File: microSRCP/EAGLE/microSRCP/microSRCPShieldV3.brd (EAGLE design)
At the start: 66.7 x 55.9 mm, 41 parts

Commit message: Feinkorrekturen
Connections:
- net S$10 renamed S$1
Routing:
- net GND: track 158.0 -> 159.5 mm
- net V5O: track 212.7 -> 212.1 mm
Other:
- board text added: "https://github.com/mc-b/microSRCP/wiki"
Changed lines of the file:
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@@
 <wire x1="66.675" y1="55.88" x2="0" y2="55.88" width="0.4064" layer="20"/>
 <wire x1="0" y1="55.88" x2="0" y2="0" width="0.4064" layer="20"/>
+<text x="19.685" y="48.26" size="1.27" layer="25">https://github.com/mc-b/microSRCP/wiki</text>
 </plain>
 <attributes>
@@
 <wire x1="12.7" y1="8.89" x2="5.08" y2="8.89" width="0.4064" layer="1"/>
 <wire x1="5.08" y1="8.89" x2="5.08" y2="10.16" width="0.4064" layer="1"/>
-<contactref element="LD4" pad="K"/>
-<wire x1="54.61" y1="20.32" x2="57.15" y2="27.94" width="0.4064" layer="1"/>
-<wire x1="57.15" y1="27.94" x2="53.34" y2="27.94" width="0.4064" layer="1"/>
-<contactref element="~LD5" pad="K"/>
-<wire x1="53.34" y1="27.94" x2="48.26" y2="27.94" width="0.4064" layer="1"/>
-<contactref element="~LD6" pad="K"/>
-<wire x1="48.26" y1="27.94" x2="43.18" y2="27.94" width="0.4064" layer="1"/>
-<contactref element="LD7" pad="K"/>
-<wire x1="43.18" y1="27.94" x2="38.1" y2="27.94" width="0.4064" layer="1"/>
+<wire x1="54.61" y1="20.32" x2="57.15" y2="20.32" width="0.4064" layer="1"/>
+<wire x1="57.15" y1="20.32" x2="57.15" y2="27.94" width="0.4064" layer="1"/>
+<contactref element="D0" pad="3"/>
 <wire x1="57.15" y1="27.94" x2="57.15" y2="33.02" width="0.4064" layer="1"/>
-<contactref element="D0" pad="3"/>
 <wire x1="57.15" y1="33.02" x2="57.15" y2="38.1" width="0.4064" layer="1"/>
 <wire x1="57.15" y1="38.1" x2="54.61" y2="38.1" width="0.4064" layer="1"/>
@@
 <contactref element="I2C" pad="4"/>
 <wire x1="57.15" y1="33.02" x2="59.69" y2="33.02" width="0.4064" layer="1"/>
+<contactref element="LD4" pad="K"/>
+<contactref element="~LD5" pad="K"/>
+<wire x1="53.34" y1="27.94" x2="48.26" y2="27.94" width="0.4064" layer="1"/>
+<contactref element="~LD6" pad="K"/>
+<wire x1="48.26" y1="27.94" x2="43.18" y2="27.94" width="0.4064" layer="1"/>
+<contactref element="LD7" pad="K"/>
+<wire x1="43.18" y1="27.94" x2="38.1" y2="27.94" width="0.4064" layer="1"/>
+<wire x1="53.34" y1="27.94" x2="57.15" y2="27.94" width="0.4064" layer="1"/>
 <contactref element="I2C-2" pad="4"/>
-<wire x1="54.61" y1="20.32" x2="59.69" y2="17.78" width="0.4064" layer="1"/>
+<wire x1="57.15" y1="20.32" x2="57.15" y2="17.78" width="0.4064" layer="1"/>
+<wire x1="57.15" y1="17.78" x2="59.69" y2="17.78" width="0.4064" layer="1"/>
 </signal>
 <signal name="V5O">
@@
 <wire x1="52.07" y1="17.78" x2="54.61" y2="17.78" width="0.4064" layer="1"/>
 <wire x1="39.37" y1="17.78" x2="41.91" y2="17.78" width="0.4064" layer="1"/>
-<wire x1="54.61" y1="17.78" x2="55.88" y2="17.78" width="0.4064" layer="16"/>
-<wire x1="55.88" y1="17.78" x2="57.15" y2="19.05" width="0.4064" layer="16"/>
-<wire x1="57.15" y1="19.05" x2="57.15" y2="30.48" width="0.4064" layer="16"/>
+<wire x1="54.61" y1="17.78" x2="57.15" y2="17.78" width="0.4064" layer="16"/>
+<wire x1="57.15" y1="17.78" x2="57.15" y2="30.48" width="0.4064" layer="16"/>
 <contactref element="D0" pad="2"/>
 <wire x1="57.15" y1="30.48" x2="57.15" y2="40.64" width="0.4064" layer="16"/>
@@
 <wire x1="11.43" y1="53.34" x2="11.43" y2="50.8" width="0.4064" layer="1"/>
 <contactref element="I2C-2" pad="3"/>
-<wire x1="57.15" y1="19.05" x2="57.15" y2="17.78" width="0.4064" layer="16"/>
 <wire x1="57.15" y1="17.78" x2="59.69" y2="15.24" width="0.4064" layer="16"/>
 <contactref element="I2C" pad="3"/>
@@
 <contactref element="LD4" pad="A"/>
 <wire x1="44.45" y1="35.56" x2="53.34" y2="30.48" width="0.4064" layer="16"/>
-</signal>
-<signal name="S$10">
-<contactref element="R2" pad="P$1"/>
-<contactref element="~LD5" pad="A"/>
-<wire x1="41.91" y1="35.56" x2="48.26" y2="30.48" width="0.4064" layer="16"/>
 </signal>
 <signal name="S$11">
@@
 <wire x1="15.24" y1="38.1" x2="15.24" y2="40.64" width="0.4064" layer="16"/>
 </signal>
+<signal name="S$1">
+<contactref element="R2" pad="P$1"/>
+<contactref element="~LD5" pad="A"/>
+<wire x1="41.91" y1="35.56" x2="46.99" y2="30.48" width="0.4064" layer="16"/>
+<wire x1="46.99" y1="30.48" x2="48.26" y2="30.48" width="0.4064" layer="16"/>
+</signal>
 </signals>

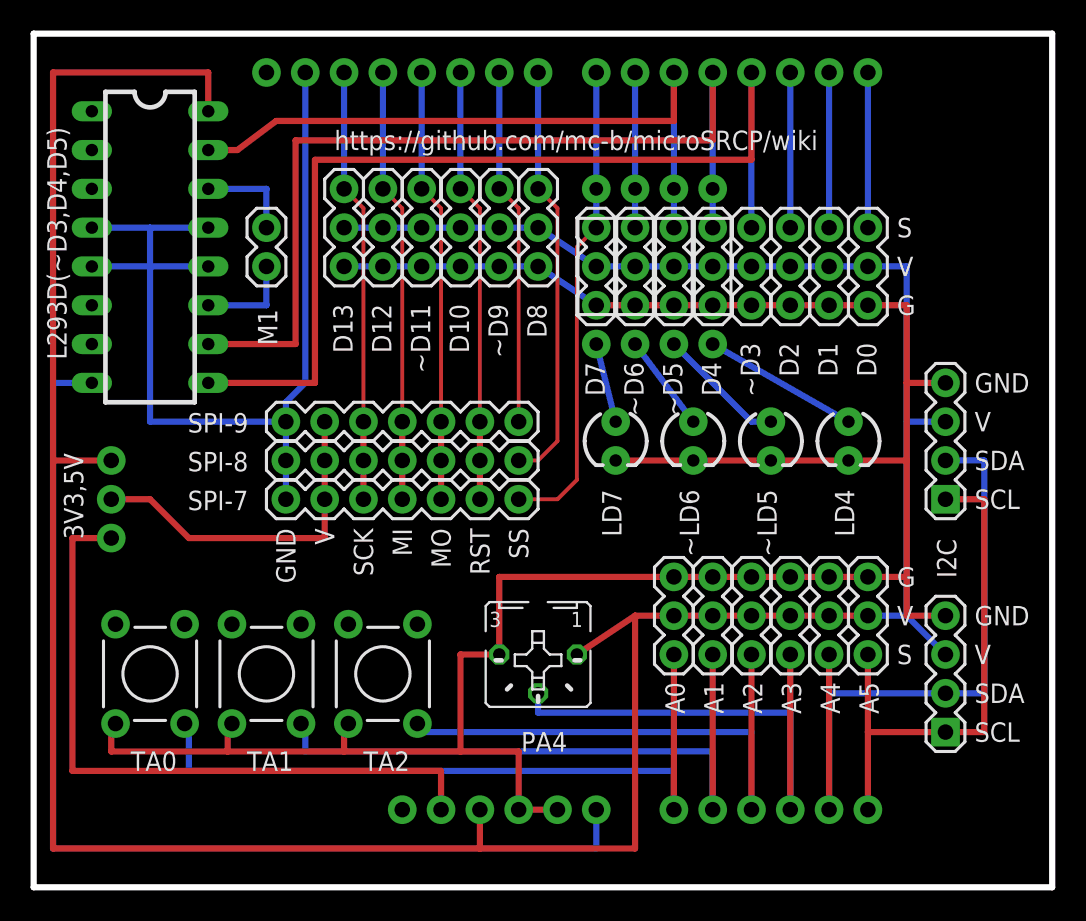
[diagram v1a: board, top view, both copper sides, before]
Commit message: V3 mit gleicher Pin-Belegung wie V2 plus SPI Anschluessen
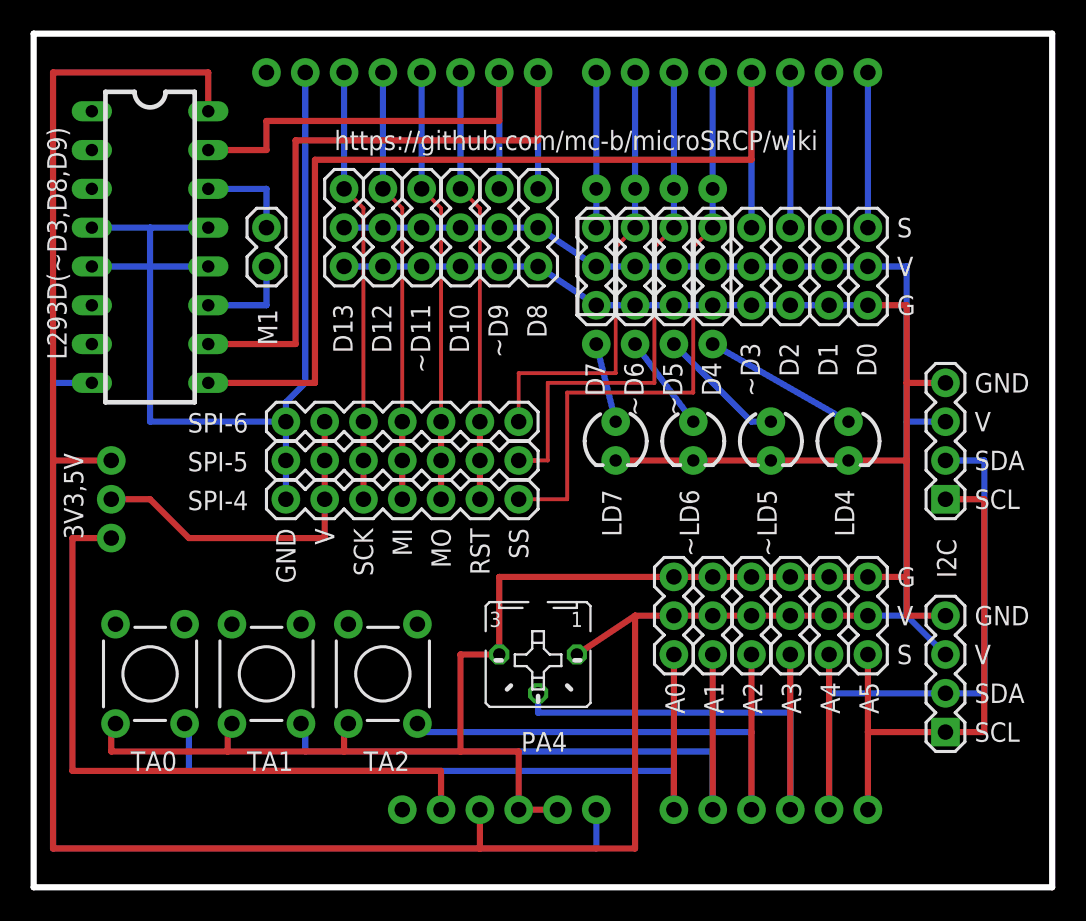
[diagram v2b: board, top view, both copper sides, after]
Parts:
- renumbered L293D(~D3,D4,D5) to L293D(~D3,D8,D9), SPI-7 to SPI-4, SPI-8 to SPI-5, SPI-9 to SPI-6
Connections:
- removed net S4: D4.1, E$1.D4, L293D(~D3,D8,D9).10, R3.P$2
- removed net S9: E$1.D9, SPI-6.7, ~D9.1
- new net S$3: E$1.D9, L293D(~D3,D8,D9).15, ~D9.1
- new net S$4: D4.1, E$1.D4, R3.P$2, SPI-4.7
- net S5: now also SPI-5.7; no longer L293D(~D3,D8,D9).15
- net S6: now also SPI-6.7
- net S7: no longer SPI-4.7
- net S8: now also L293D(~D3,D8,D9).10; no longer SPI-5.7
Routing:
- net S4: track 61.0 -> 0.00 mm
- net S$4: track 0.00 -> 39.9 mm
- net S$3: track 0.00 -> 31.8 mm
- net S9: track 23.4 -> 0.00 mm
- net S7: track 31.5 -> 10.2 mm
- net S6: track 10.2 -> 29.7 mm
- net S8: track 27.7 -> 47.0 mm
- net S5: track 44.5 -> 36.1 mm

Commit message: Massenflaechen angefuegt
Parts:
- renumbered D10 to ~D10
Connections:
- removed net GND1: E$1.GND@2, L293D(~D3,D8,D9).12, L293D(~D3,D8,D9).13, L293D(~D3,D8,D9).4, L293D(~D3,D8,D9).5, SPI-4.1, SPI-5.1, SPI-6.1
- net GND: now also E$1.GND@2, L293D(~D3,D8,D9).12, L293D(~D3,D8,D9).13, L293D(~D3,D8,D9).4, L293D(~D3,D8,D9).5, SPI-4.1, SPI-5.1, SPI-6.1
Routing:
- net GND: track 159.5 -> 227.4 mm
- net GND1: track 65.3 -> 0.00 mm
- added copper zone on layer 1, net GND
- added copper zone on layer 16, net GND
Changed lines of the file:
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@@
 <layers>
 <layer number="1" name="Top" color="4" fill="1" visible="yes" active="yes"/>
-<layer number="16" name="Bottom" color="1" fill="1" visible="yes" active="yes"/>
+<layer number="16" name="Bottom" color="1" fill="1" visible="no" active="yes"/>
 <layer number="17" name="Pads" color="2" fill="1" visible="yes" active="yes"/>
 <layer number="18" name="Vias" color="2" fill="1" visible="yes" active="yes"/>
@@
 <attribute name="VALUE" x="27.305" y="46.99" size="1.27" layer="27" rot="R270"/>
 </element>
-<element name="D10" library="SparkFun-Connectors" package="1X03" value="" x="27.94" y="45.72" smashed="yes" rot="R270">
+<element name="~D10" library="SparkFun-Connectors" package="1X03" value="" x="27.94" y="45.72" smashed="yes" rot="R270">
 <attribute name="NAME" x="27.2288" y="38.1762" size="1.27" layer="25" ratio="10" rot="R270"/>
 <attribute name="VALUE" x="24.765" y="46.99" size="1.27" layer="27" rot="R270"/>
@@
 <contactref element="~D9" pad="3"/>
 <wire x1="33.02" y1="40.64" x2="30.48" y2="40.64" width="0.4064" layer="16"/>
-<contactref element="D10" pad="3"/>
+<contactref element="~D10" pad="3"/>
 <wire x1="30.48" y1="40.64" x2="27.94" y2="40.64" width="0.4064" layer="16"/>
 <contactref element="~D11" pad="3"/>
@@
 <wire x1="22.86" y1="40.64" x2="20.32" y2="40.64" width="0.4064" layer="16"/>
 <wire x1="39.37" y1="38.1" x2="36.83" y2="38.1" width="0.4064" layer="16"/>
+<polygon width="0.4064" layer="16">
+<vertex x="0.635" y="54.61"/>
+<vertex x="0.635" y="1.27"/>
+<vertex x="65.405" y="1.27"/>
+<vertex x="65.405" y="54.61"/>
+</polygon>
+<contactref element="E$1" pad="GND@2"/>
+<wire x1="17.78" y1="53.34" x2="17.78" y2="40.64" width="0.4064" layer="16"/>
+<contactref element="SPI-6" pad="1"/>
+<wire x1="17.78" y1="40.64" x2="17.78" y2="33.02" width="0.4064" layer="16"/>
+<wire x1="17.78" y1="33.02" x2="16.51" y2="31.75" width="0.4064" layer="16"/>
+<wire x1="16.51" y1="31.75" x2="16.51" y2="30.48" width="0.4064" layer="16"/>
+<contactref element="SPI-5" pad="1"/>
+<wire x1="16.51" y1="30.48" x2="16.51" y2="27.94" width="0.4064" layer="16"/>
+<contactref element="SPI-4" pad="1"/>
+<wire x1="16.51" y1="27.94" x2="16.51" y2="25.4" width="0.4064" layer="16"/>
+<wire x1="16.51" y1="30.48" x2="7.62" y2="30.48" width="0.4064" layer="16"/>
+<wire x1="7.62" y1="30.48" x2="7.62" y2="40.64" width="0.4064" layer="16"/>
+<contactref element="L293D(~D3,D8,D9)" pad="12"/>
+<wire x1="11.43" y1="40.64" x2="7.62" y2="40.64" width="0.4064" layer="16"/>
+<contactref element="L293D(~D3,D8,D9)" pad="13"/>
+<contactref element="L293D(~D3,D8,D9)" pad="4"/>
+<wire x1="11.43" y1="43.18" x2="7.62" y2="43.18" width="0.4064" layer="16"/>
+<wire x1="3.81" y1="43.18" x2="7.62" y2="43.18" width="0.4064" layer="16"/>
+<wire x1="7.62" y1="43.18" x2="7.62" y2="40.64" width="0.4064" layer="16"/>
+<contactref element="L293D(~D3,D8,D9)" pad="5"/>
+<wire x1="7.62" y1="40.64" x2="3.81" y2="40.64" width="0.4064" layer="16"/>
+<wire x1="17.78" y1="40.64" x2="20.32" y2="40.64" width="0.4064" layer="16"/>
+<polygon width="0.4064" layer="1">
+<vertex x="0.635" y="55.245"/>
+<vertex x="0.635" y="1.27"/>
+<vertex x="65.405" y="1.27"/>
+<vertex x="65.405" y="1.905"/>
+<vertex x="65.405" y="55.245"/>
+</polygon>
 </signal>
 <signal name="V5O">
@@
 <contactref element="~D9" pad="2"/>
 <wire x1="33.02" y1="43.18" x2="30.48" y2="43.18" width="0.4064" layer="16"/>
-<contactref element="D10" pad="2"/>
+<contactref element="~D10" pad="2"/>
 <wire x1="30.48" y1="43.18" x2="27.94" y2="43.18" width="0.4064" layer="16"/>
 <contactref element="~D11" pad="2"/>
@@
 <wire x1="39.37" y1="53.34" x2="39.37" y2="43.18" width="0.4064" layer="16"/>
 <contactref element="~D6" pad="1"/>
-<wire x1="39.37" y1="43.18" x2="39.37" y2="45.72" width="0" layer="19" extent="16-16"/>
 <wire x1="39.37" y1="43.18" x2="38.1" y2="41.91" width="0.254" layer="1"/>
 <wire x1="38.1" y1="41.91" x2="38.1" y2="33.655" width="0.254" layer="1"/>
@@
 <contactref element="SPI-6" pad="7"/>
 <wire x1="31.75" y1="33.655" x2="31.75" y2="30.48" width="0.254" layer="1"/>
+<wire x1="39.37" y1="43.18" x2="39.37" y2="45.72" width="0" layer="19" extent="16-16"/>
 </signal>
 <signal name="S5">
@@
 <wire x1="41.91" y1="53.34" x2="41.91" y2="43.18" width="0.4064" layer="16"/>
 <contactref element="~D5" pad="1"/>
-<wire x1="41.91" y1="43.18" x2="41.91" y2="45.72" width="0" layer="19" extent="1-1"/>
 <wire x1="41.91" y1="43.18" x2="40.64" y2="41.91" width="0.254" layer="1"/>
 <wire x1="40.64" y1="41.91" x2="40.64" y2="33.02" width="0.254" layer="1"/>
@@
 <wire x1="33.02" y1="27.94" x2="31.75" y2="27.94" width="0.254" layer="1"/>
 <wire x1="33.655" y1="27.94" x2="31.75" y2="27.94" width="0.254" layer="1"/>
+<wire x1="41.91" y1="43.18" x2="41.91" y2="45.72" width="0" layer="19" extent="16-16"/>
 </signal>
 <signal name="S$4">
@@
 <wire x1="44.45" y1="53.34" x2="44.45" y2="43.18" width="0.4064" layer="16"/>
 <contactref element="D4" pad="1"/>
-<wire x1="44.45" y1="43.18" x2="44.45" y2="45.72" width="0" layer="19" extent="1-1"/>
 <wire x1="44.45" y1="43.18" x2="43.18" y2="41.91" width="0.254" layer="1"/>
 <wire x1="43.18" y1="41.91" x2="43.18" y2="32.385" width="0.254" layer="1"/>
@@
 <contactref element="SPI-4" pad="7"/>
 <wire x1="34.925" y1="25.4" x2="31.75" y2="25.4" width="0.254" layer="1"/>
+<wire x1="44.45" y1="43.18" x2="44.45" y2="45.72" width="0" layer="19" extent="16-16"/>
 </signal>
 <signal name="S3">
@@
 <signal name="S10">
 <contactref element="E$1" pad="D10"/>
-<contactref element="D10" pad="1"/>
+<contactref element="~D10" pad="1"/>
 <wire x1="27.94" y1="53.34" x2="27.94" y2="45.72" width="0.4064" layer="16"/>
 <wire x1="27.94" y1="45.72" x2="29.21" y2="44.45" width="0.254" layer="1"/>
@@
 <wire x1="1.27" y1="33.02" x2="3.81" y2="33.02" width="0.4064" layer="16"/>
 </signal>
-<signal name="GND1">
-<contactref element="E$1" pad="GND@2"/>
-<wire x1="17.78" y1="53.34" x2="17.78" y2="33.02" width="0.4064" layer="16"/>
-<contactref element="SPI-6" pad="1"/>
-<wire x1="17.78" y1="33.02" x2="16.51" y2="31.75" width="0.4064" layer="16"/>
-<wire x1="16.51" y1="31.75" x2="16.51" y2="30.48" width="0.4064" layer="16"/>
-<contactref element="SPI-5" pad="1"/>
-<wire x1="16.51" y1="30.48" x2="16.51" y2="27.94" width="0.4064" layer="16"/>
-<contactref element="SPI-4" pad="1"/>
-<wire x1="16.51" y1="27.94" x2="16.51" y2="25.4" width="0.4064" layer="16"/>
-<wire x1="16.51" y1="30.48" x2="7.62" y2="30.48" width="0.4064" layer="16"/>
-<wire x1="7.62" y1="30.48" x2="7.62" y2="40.64" width="0.4064" layer="16"/>
-<contactref element="L293D(~D3,D8,D9)" pad="12"/>
-<wire x1="11.43" y1="40.64" x2="7.62" y2="40.64" width="0.4064" layer="16"/>
-<contactref element="L293D(~D3,D8,D9)" pad="13"/>
-<contactref element="L293D(~D3,D8,D9)" pad="4"/>
-<wire x1="11.43" y1="43.18" x2="7.62" y2="43.18" width="0.4064" layer="16"/>
-<wire x1="3.81" y1="43.18" x2="7.62" y2="43.18" width="0.4064" layer="16"/>
-<wire x1="7.62" y1="43.18" x2="7.62" y2="40.64" width="0.4064" layer="16"/>
-<contactref element="L293D(~D3,D8,D9)" pad="5"/>
-<wire x1="7.62" y1="40.64" x2="3.81" y2="40.64" width="0.4064" layer="16"/>
-</signal>
 <signal name="SM1-L">

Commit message: Detailkorrekturen
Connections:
- removed net S$26: 3V3,5V.2, SPI-4.2, SPI-5.2, SPI-6.2
- new net S$2: 3V3,5V.2, SPI-4.6, SPI-5.6, SPI-6.6
- net GND: now also SPI-4.7, SPI-5.7, SPI-6.7; no longer SPI-4.1, SPI-5.1, SPI-6.1
- net S$4: now also SPI-4.5; no longer SPI-4.7
- net S10: now also SPI-4.4, SPI-5.4, SPI-6.4; no longer SPI-4.6, SPI-5.6, SPI-6.6
- net S11: now also SPI-4.3, SPI-5.3, SPI-6.3; no longer SPI-4.5, SPI-5.5, SPI-6.5
- net S12: now also SPI-4.2, SPI-5.2, SPI-6.2; no longer SPI-4.4, SPI-5.4, SPI-6.4
- net S13: now also SPI-4.1, SPI-5.1, SPI-6.1; no longer SPI-4.3, SPI-5.3, SPI-6.3
- net S5: now also SPI-5.5; no longer SPI-5.7
- net S6: now also SPI-6.5; no longer SPI-6.7
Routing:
- net S$2: track 0.00 -> 32.5 mm
- net S$26: track 22.6 -> 0.00 mm
- net GND: track 227.4 -> 245.2 mm
- net S$4: track 39.9 -> 44.2 mm
- net S6: track 29.7 -> 33.2 mm
- net S5: track 36.1 -> 39.2 mm
- net S3: track 66.0 -> 63.6 mm
- net S8: track 47.0 -> 45.0 mm
- net S11: track 28.5 -> 30.4 mm
- net S10: track 28.5 -> 30.4 mm
- net S13: track 28.5 -> 30.4 mm
- net S12: track 28.5 -> 30.4 mm
- net SM1R: track 6.35 -> 5.08 mm
- net SM1-L: track 6.35 -> 5.08 mm
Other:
- board text added: "SCK MI MO RST SS V GND"
- board text removed: "GND V SCK MI MO RST SS"
